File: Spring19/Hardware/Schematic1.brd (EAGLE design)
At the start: 72.4 x 59.4 mm, 18 parts

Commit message: Add through holes for plug
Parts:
- added X1: SSW-101-02-G-D, con-samtec:SSW-101-02-G-D
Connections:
- new net N$11: RELAYRIGHT.6, X1.1
- new net N$13: RELAYRIGHT.2, X1.2
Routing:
- net N$13: track 0.00 -> 6.66 mm
- net N$11: track 0.00 -> 6.66 mm
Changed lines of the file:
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@@
 <attribute name="VALUE" x="102.87" y="69.342" size="0.6096" layer="27" font="vector" ratio="20" rot="R180" align="top-center"/>
+</element>
+<element name="X1" library="con-samtec" library_urn="urn:adsk.eagle:library:184" package="SSW-101-02-G-D" value="SSW-101-02-G-D" x="99.06" y="54.61" smashed="yes" rot="R90">
+<attribute name="MF" value="Samtec Inc." x="99.06" y="54.61" size="1.778" layer="27" rot="R90" display="off"/>
+<attribute name="MPN" value="SSW-101-02-G-D" x="99.06" y="54.61" size="1.778" layer="27" rot="R90" display="off"/>
+<attribute name="NAME" x="101.6" y="52.705" size="1.27" layer="25" rot="R180"/>
+<attribute name="OC_FARNELL" value="unknown" x="99.06" y="54.61" size="1.778" layer="27" rot="R90" display="off"/>
+<attribute name="OC_NEWARK" value="82P1456" x="99.06" y="54.61" size="1.778" layer="27" rot="R90" display="off"/>
+<attribute name="VALUE" x="101.6" y="57.785" size="1.27" layer="27" rot="R180"/>
 </element>
 </elements>
@@
 <wire x1="88.2396" y1="50.1396" x2="90.8304" y2="50.1396" width="0.3048" layer="1"/>
 <wire x1="90.8304" y1="50.1396" x2="90.8812" y2="50.0888" width="0.3048" layer="1"/>
-<wire x1="90.8812" y1="50.0888" x2="91.44" y2="50.0888" width="0.3048" layer="1"/>
-<wire x1="91.44" y1="50.0888" x2="97.79" y2="56.4388" width="0.3048" layer="1"/>
 <wire x1="53.34" y1="65.62" x2="56.3" y2="68.58" width="0.3048" layer="1"/>
 <wire x1="68.326" y1="68.58" x2="73.406" y2="73.66" width="0.3048" layer="1"/>
 <wire x1="56.3" y1="68.58" x2="68.326" y2="68.58" width="0.3048" layer="1"/>
-<wire x1="97.79" y1="56.4388" x2="107.2388" y2="56.4388" width="0.3048" layer="1"/>
-<wire x1="107.2388" y1="56.4388" x2="109.22" y2="58.42" width="0.3048" layer="1"/>
-<wire x1="109.22" y1="58.42" x2="109.22" y2="62.23" width="0.3048" layer="1"/>
 <wire x1="109.22" y1="62.23" x2="106.68" y2="64.77" width="0.3048" layer="1"/>
 <wire x1="103.72" y1="68.58" x2="106.68" y2="65.62" width="0.3048" layer="1"/>
 <wire x1="106.68" y1="65.62" x2="106.68" y2="64.77" width="0.3048" layer="1"/>
+<wire x1="90.8812" y1="50.0888" x2="98.97801875" y2="50.0888" width="0.3048" layer="1"/>
+<wire x1="98.97801875" y1="50.0888" x2="104.76921875" y2="55.88" width="0.3048" layer="1"/>
+<wire x1="104.76921875" y1="55.88" x2="106.68" y2="55.88" width="0.3048" layer="1"/>
+<wire x1="106.68" y1="55.88" x2="109.22" y2="58.42" width="0.3048" layer="1"/>
+<wire x1="109.22" y1="58.42" x2="109.22" y2="62.23" width="0.3048" layer="1"/>
 </signal>
 <signal name="+3V3">
@@
 <wire x1="95.25" y1="68.58" x2="102.02" y2="68.58" width="0.3048" layer="1"/>
 </signal>
+<signal name="N$11">
+<contactref element="RELAYRIGHT" pad="6"/>
+<contactref element="X1" pad="1"/>
+<wire x1="100.33" y1="54.61" x2="100.33" y2="55.88" width="0.3048" layer="1"/>
+<wire x1="100.33" y1="55.88" x2="104.14" y2="59.69" width="0.3048" layer="1"/>
+</signal>
+<signal name="N$13">
+<contactref element="X1" pad="2"/>
+<contactref element="RELAYRIGHT" pad="2"/>
+<wire x1="93.98" y1="59.69" x2="97.79" y2="55.88" width="0.3048" layer="1"/>
+<wire x1="97.79" y1="55.88" x2="97.79" y2="54.61" width="0.3048" layer="1"/>
+</signal>
 </signals>

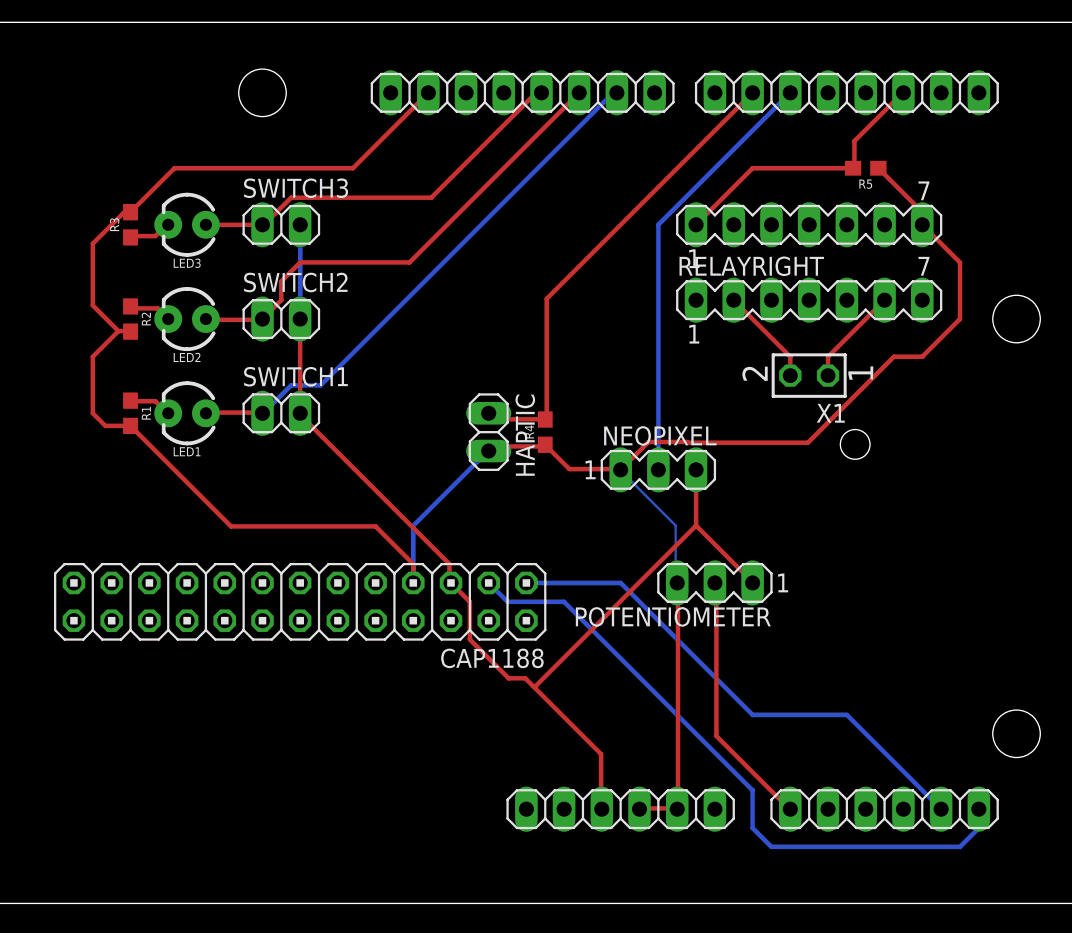
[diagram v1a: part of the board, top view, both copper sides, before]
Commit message: Single sided board with airwires
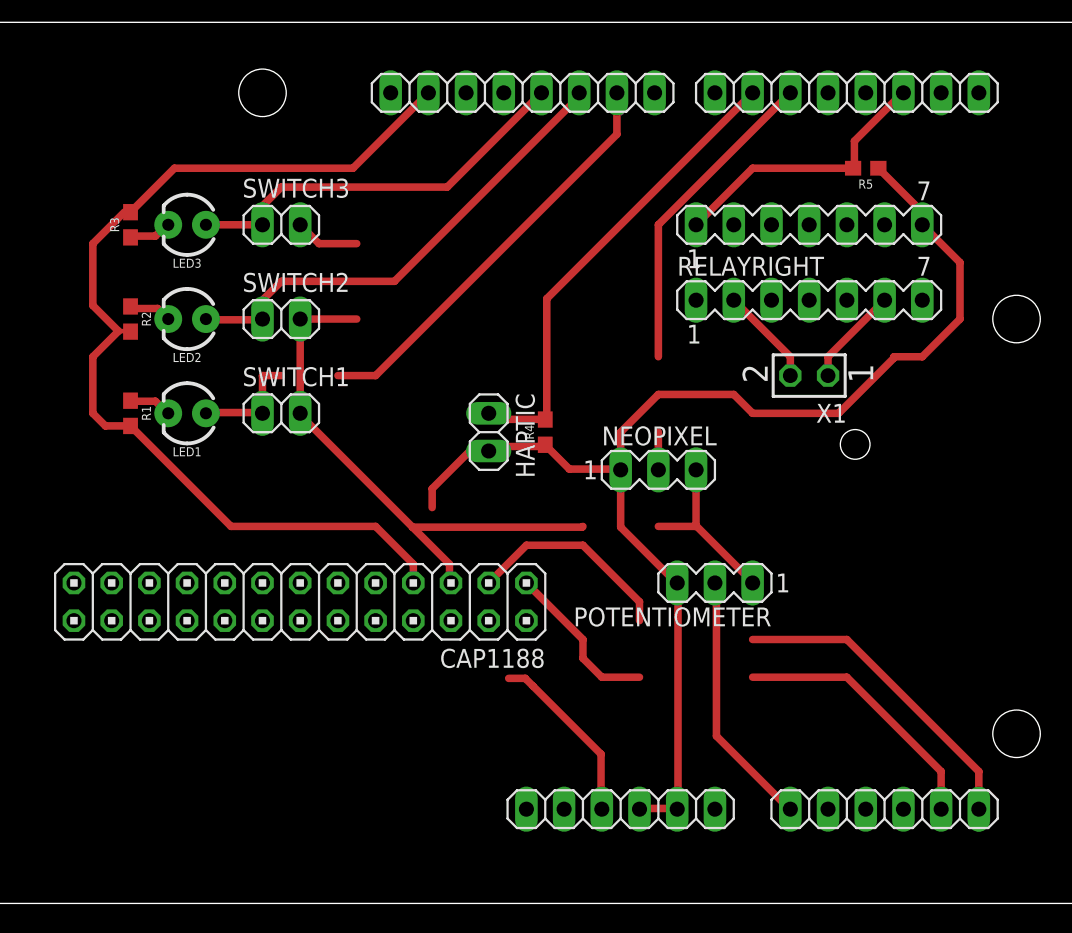
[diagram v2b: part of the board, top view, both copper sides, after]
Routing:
- net VCC: track 73.2 -> 65.7 mm
- net N$8: track 44.2 -> 37.4 mm
- net N$6: track 30.4 -> 24.1 mm
- net N$7: track 35.0 -> 29.6 mm
- net GND: track 157.6 -> 155.7 mm
- net N$10: track 26.3 -> 27.6 mm
- net N$5: track 36.7 -> 37.8 mm

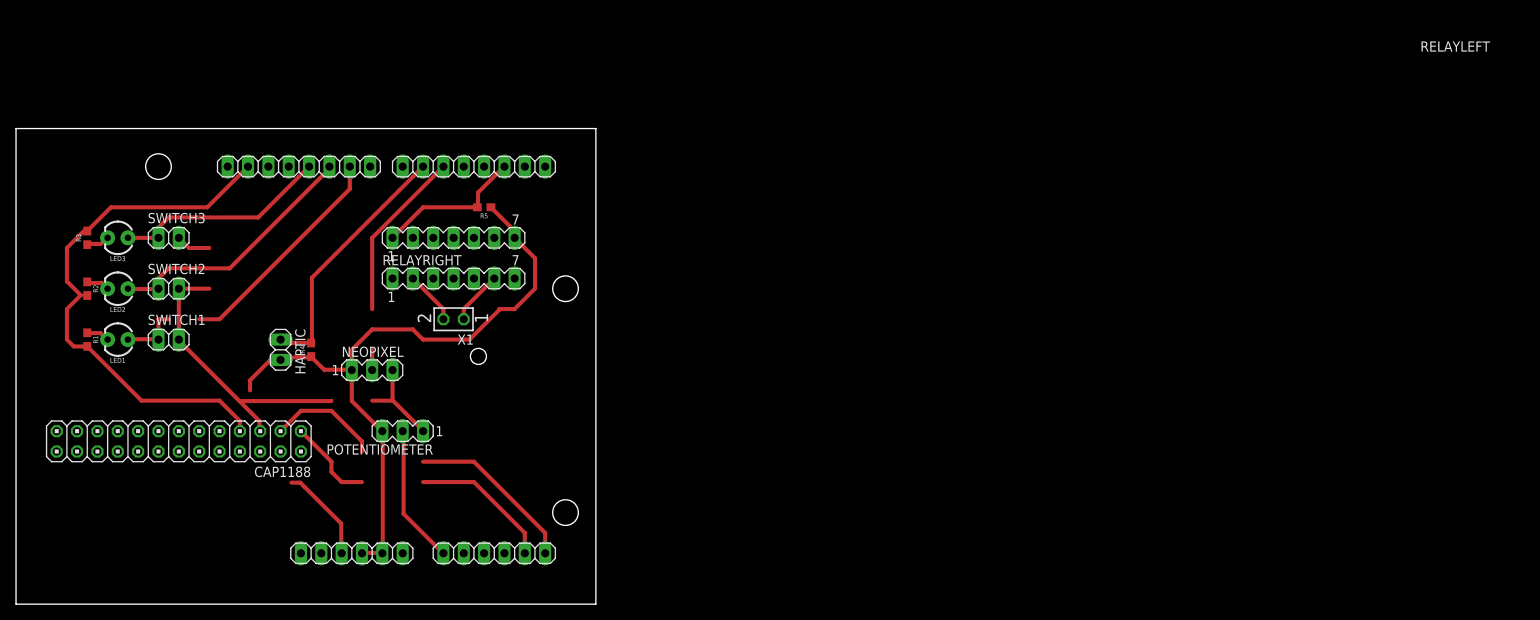
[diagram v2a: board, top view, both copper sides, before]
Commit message: Fix relay width
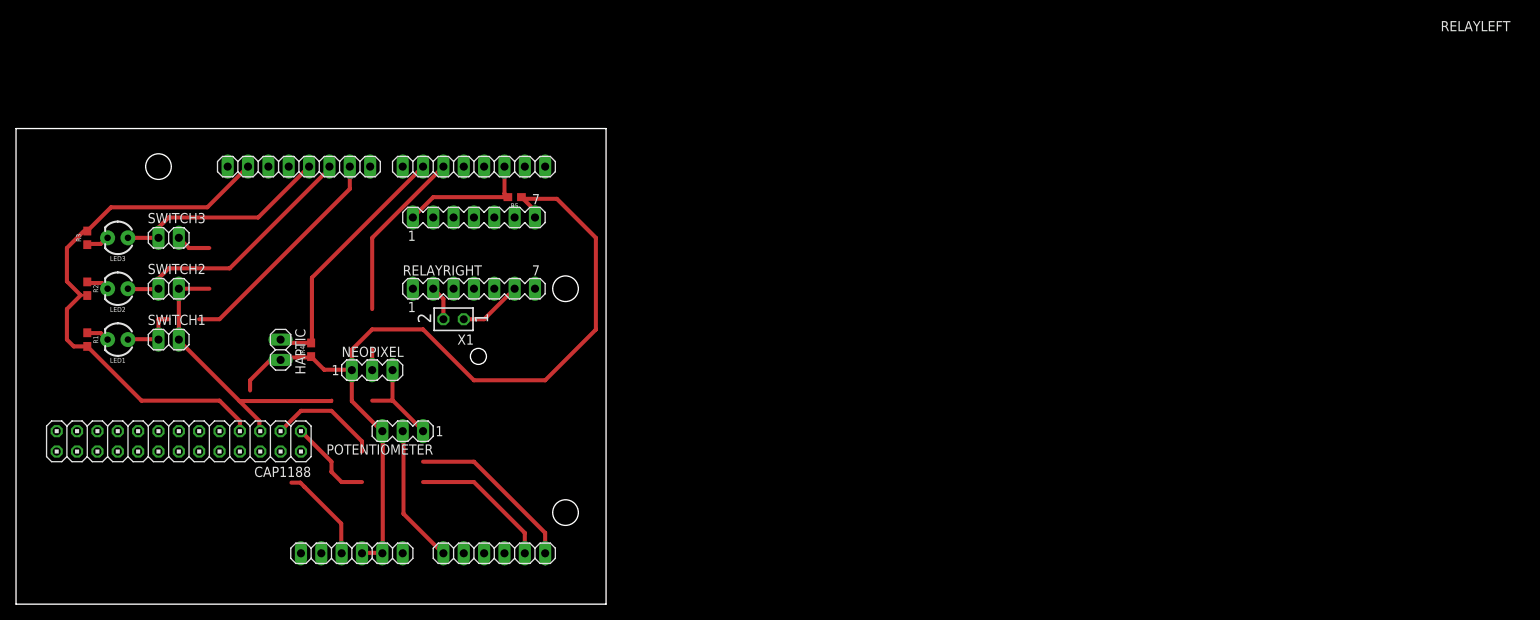
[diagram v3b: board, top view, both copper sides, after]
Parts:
- moved R5 4.02 mm to (106.7, 69.8)
- moved RELAYLEFT 3.59 mm to (101.6, 67.3)
- moved RELAYRIGHT 2.84 mm to (101.6, 58.4)
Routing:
- net GND: track 155.7 -> 178.7 mm
- net N$13: track 6.66 -> 4.34 mm
- net N$14: track 18.7 -> 17.0 mm
- net N$11: track 6.66 -> 7.93 mm
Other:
- board size 72.4 x 59.4 mm -> 73.6 x 59.4 mm

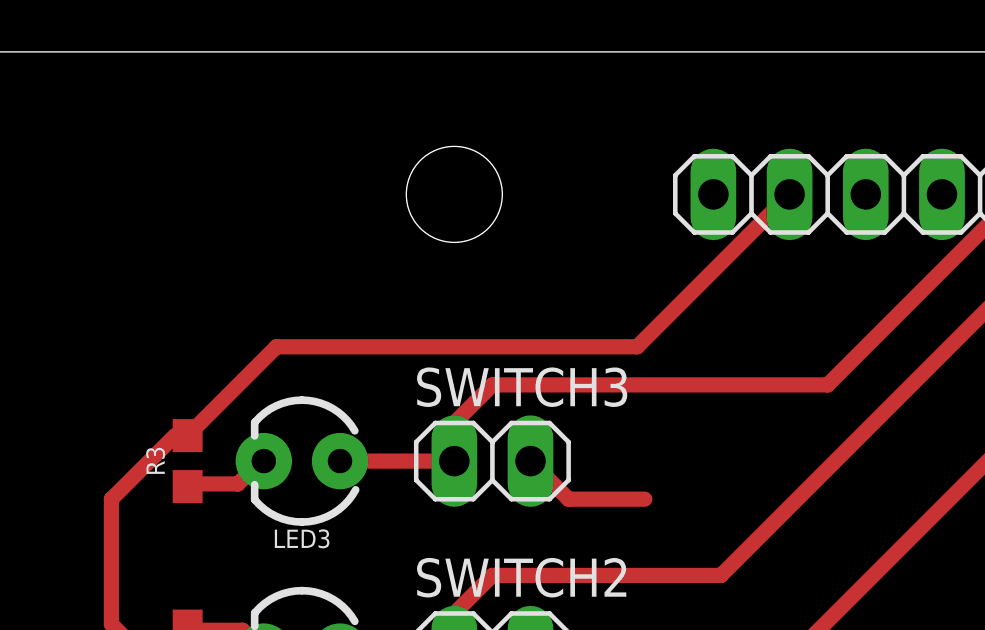
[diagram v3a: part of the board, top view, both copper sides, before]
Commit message: Adjst trace widths
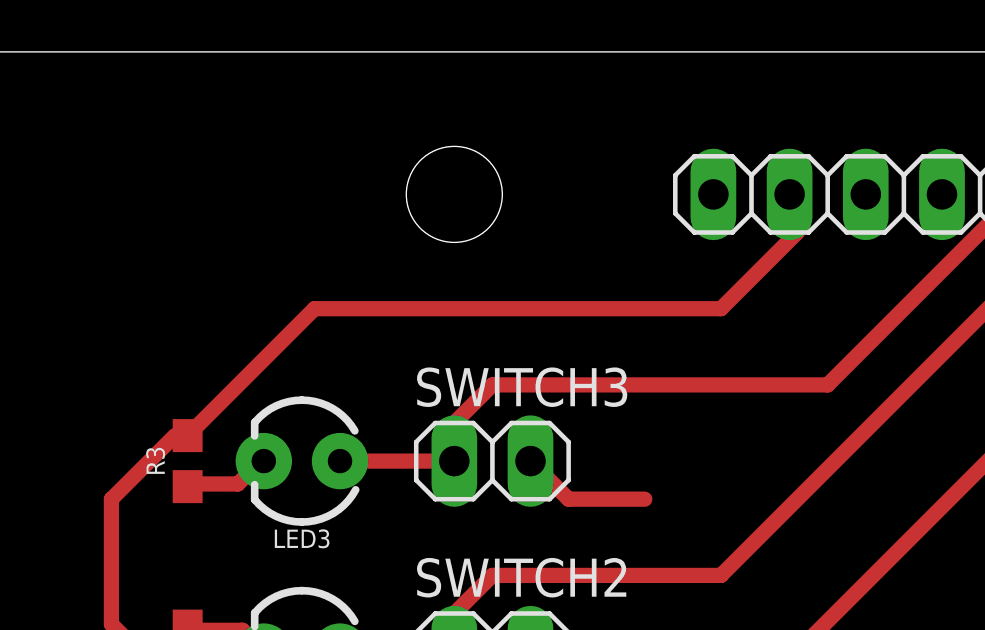
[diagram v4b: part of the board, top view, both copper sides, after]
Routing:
- net GND: track 178.7 -> 179.8 mm
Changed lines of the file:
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@@
 <wire x1="50.8" y1="59.3344" x2="50.8" y2="63.5" width="0.508" layer="1"/>
 <wire x1="50.8" y1="63.5" x2="52.92" y2="65.62" width="0.508" layer="1"/>
-<wire x1="53.34" y1="65.62" x2="56.3" y2="68.58" width="0.508" layer="1"/>
-<wire x1="68.326" y1="68.58" x2="73.406" y2="73.66" width="0.508" layer="1"/>
-<wire x1="56.3" y1="68.58" x2="68.326" y2="68.58" width="0.508" layer="1"/>
 <wire x1="77.47" y1="49.53" x2="76.2" y2="49.53" width="0.508" layer="1"/>
 <wire x1="76.2" y1="49.53" x2="73.66" y2="46.99" width="0.508" layer="1"/>
@@
 <wire x1="111.95" y1="69.64" x2="107.74" y2="69.64" width="0.508" layer="1"/>
 <wire x1="110.49" y1="46.99" x2="116.82" y2="53.32" width="0.508" layer="1"/>
+<wire x1="71.12" y1="69.85" x2="73.66" y2="72.39" width="0.508" layer="1"/>
+<wire x1="73.66" y1="72.39" x2="73.406" y2="72.644" width="0.508" layer="1"/>
+<wire x1="73.406" y1="72.644" x2="73.406" y2="73.66" width="0.508" layer="1"/>
+<wire x1="53.34" y1="65.62" x2="57.57" y2="69.85" width="0.508" layer="1"/>
+<wire x1="57.57" y1="69.85" x2="71.12" y2="69.85" width="0.508" layer="1"/>
 <wire x1="72.39" y1="41.91" x2="73.66" y2="45.72" width="0" layer="19" extent="1-1"/>
 </signal>
